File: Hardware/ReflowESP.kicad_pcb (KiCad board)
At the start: 2 copper layers, 72 x 72 mm, 61 parts, among them J1 USB_B_Micro, J10 SSR3, J11 TC1, J12 TC2, J2 VIN, J3 PROG, J4 SERVO, J5 DISPLAY, J6 V_SSR_SEL, J7 SSR1, J8 EXT_V_SSR, J9 SSR2, Q1 BSS138, Q2 BSS138, Q3 BSS138, SW1 SW_RESET, SW2 SW_BOOT, U1 NCP1117-3.3_SOT223, U2 ESP32-WROVER-E, U3 MAX31855KASA, U4 MAX31855KASA

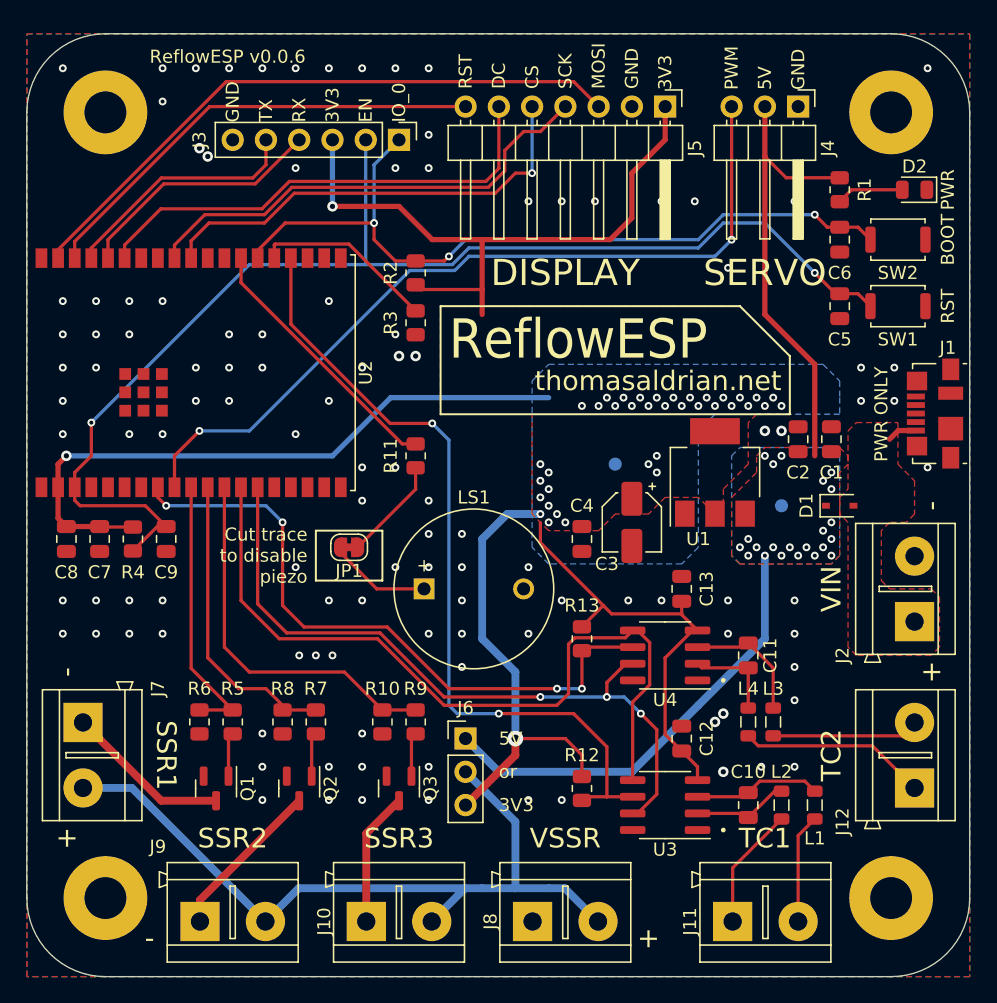
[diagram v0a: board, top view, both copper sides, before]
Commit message: Update v0.0.7
Add rotary encoder
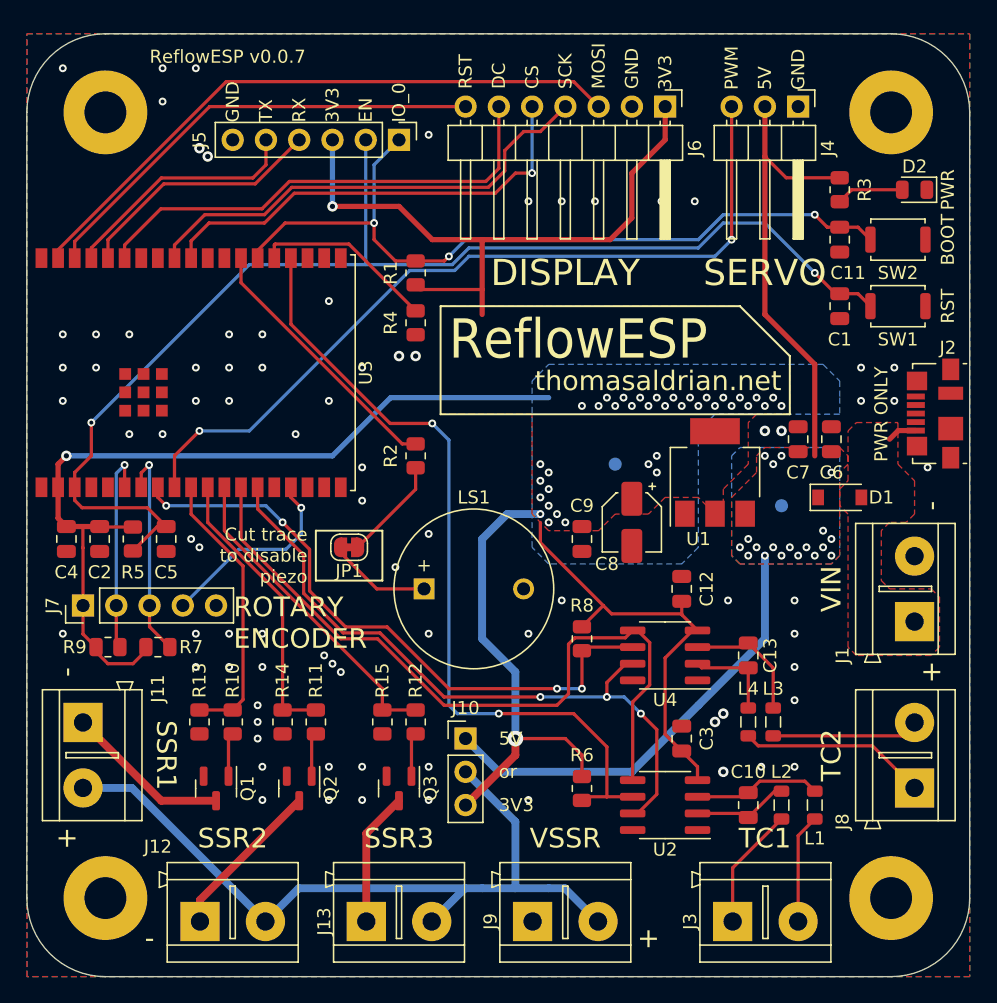
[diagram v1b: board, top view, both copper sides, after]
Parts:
- added J7: Conn_01x05, Connector_PinHeader_2.54mm:PinHeader_1x05_P2.54mm_Vertical, F.Cu at (34.3, 73.7)
- added R7: 10k, Resistor_SMD:R_0805_2012Metric, F.Cu at (40.0, 76.8)
- added R9: 10k, Resistor_SMD:R_0805_2012Metric, F.Cu at (36.2, 76.8)
- D1: footprint Diode_SMD:D_SOD-323 -> Diode_SMD:D_SOD-123
- U2: renamed from U3; footprint Package_SOIC-8:SOIC-8_3.9x4.9mm_P1.27mm -> Package_SO:SOIC-8_3.9x4.9mm_P1.27mm
- U4: footprint Package_SOIC-8:SOIC-8_3.9x4.9mm_P1.27mm -> Package_SO:SOIC-8_3.9x4.9mm_P1.27mm
- moved D1 0.64 mm to (92.1, 65.4)
- renumbered C5 to C1, C6 to C11, C13 to C12, C11 to C13, C7 to C2, C12 to C3, C8 to C4, C9 to C5, C1 to C6, C2 to C7, C3 to C8, C4 to C9, H3 to H2, H2 to H3, J2 to J1, J6 to J10, J7 to J11, J9 to J12, J10 to J13, J1 to J2, J11 to J3, J3 to J5, J5 to J6, J12 to J8, J8 to J9, R2 to R1, R5 to R10, R7 to R11, R9 to R12, R6 to R13, R8 to R14, R10 to R15, R11 to R2, R1 to R3, R3 to R4, R4 to R5, R12 to R6, R13 to R8, U2 to U3
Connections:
- U3 pad 16: MOSI -> RE_SW
- U3 pad 6: unconnected-(U2-Pad6) -> RE_A
- U3 pad 7: unconnected-(U2-Pad7) -> RE_B
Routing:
- net RE_B: track 0.00 -> 16.5 mm, vias 0 -> 1
- net RE_A: track 0.00 -> 16.0 mm, vias 0 -> 1
- net RE_SW: track 0.00 -> 15.2 mm, vias 0 -> 1
- net +3V3: track 168.6 -> 183.5 mm
- net SSR3: track 28.8 -> 24.5 mm
- net SCK: track 59.2 -> 56.4 mm
- net MISO: track 54.4 -> 51.9 mm
- net CS1: track 49.8 -> 48.0 mm
- net SSR2: track 23.1 -> 21.9 mm
- net SSR1: track 20.9 -> 21.5 mm
- net GND: vias 114 -> 81
- net +5V: vias 22 -> 19
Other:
- board text added: "ROTARY ENCODER"
